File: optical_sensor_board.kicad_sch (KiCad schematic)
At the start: 34 parts, among them J2 Conn_01x09_Socket, U1 PMW3389DM‐T3QU, U3 LM317L_SOT-89

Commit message: start TestPoint routing
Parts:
- TP1, TP10, TP11, TP12, TP13, TP14, TP15, TP16, TP2, TP3, TP4, TP5, TP6, TP7, TP8, TP9: footprint TestPoint:TestPoint_Keystone_5019_Miniature -> TestPoint:TestPoint_Pad_1.0x1.0mm
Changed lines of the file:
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@@
 			)
 		)
-		(property "Footprint" "TestPoint:TestPoint_Keystone_5019_Miniature"
+		(property "Footprint" "TestPoint:TestPoint_Pad_1.0x1.0mm"
 			(at 203.2 144.78 0)
 			(effects
@@
 			)
 		)
-		(property "Footprint" "TestPoint:TestPoint_Keystone_5019_Miniature"
+		(property "Footprint" "TestPoint:TestPoint_Pad_1.0x1.0mm"
 			(at 101.6 101.6 0)
 			(effects
@@
 			)
 		)
-		(property "Footprint" "TestPoint:TestPoint_Keystone_5019_Miniature"
+		(property "Footprint" "TestPoint:TestPoint_Pad_1.0x1.0mm"
 			(at 266.7 129.54 0)
 			(effects
@@
 			)
 		)
-		(property "Footprint" "TestPoint:TestPoint_Keystone_5019_Miniature"
+		(property "Footprint" "TestPoint:TestPoint_Pad_1.0x1.0mm"
 			(at 101.6 78.74 0)
 			(effects
@@
 			)
 		)
-		(property "Footprint" "TestPoint:TestPoint_Keystone_5019_Miniature"
+		(property "Footprint" "TestPoint:TestPoint_Pad_1.0x1.0mm"
 			(at 190.5 129.54 0)
 			(effects
@@
 			)
 		)
-		(property "Footprint" "TestPoint:TestPoint_Keystone_5019_Miniature"
+		(property "Footprint" "TestPoint:TestPoint_Pad_1.0x1.0mm"
 			(at 254 129.54 0)
 			(effects
@@
 			)
 		)
-		(property "Footprint" "TestPoint:TestPoint_Keystone_5019_Miniature"
+		(property "Footprint" "TestPoint:TestPoint_Pad_1.0x1.0mm"
 			(at 194.31 41.91 0)
 			(effects
@@
 			)
 		)
-		(property "Footprint" "TestPoint:TestPoint_Keystone_5019_Miniature"
+		(property "Footprint" "TestPoint:TestPoint_Pad_1.0x1.0mm"
 			(at 215.9 129.54 0)
 			(effects
@@
 			)
 		)
-		(property "Footprint" "TestPoint:TestPoint_Keystone_5019_Miniature"
+		(property "Footprint" "TestPoint:TestPoint_Pad_1.0x1.0mm"
 			(at 69.85 153.67 0)
 			(effects
@@
 			)
 		)
-		(property "Footprint" "TestPoint:TestPoint_Keystone_5019_Miniature"
+		(property "Footprint" "TestPoint:TestPoint_Pad_1.0x1.0mm"
 			(at 190.5 144.78 0)
 			(effects
@@
 			)
 		)
-		(property "Footprint" "TestPoint:TestPoint_Keystone_5019_Miniature"
+		(property "Footprint" "TestPoint:TestPoint_Pad_1.0x1.0mm"
 			(at 241.3 129.54 0)
 			(effects
@@
 			)
 		)
-		(property "Footprint" "TestPoint:TestPoint_Keystone_5019_Miniature"
+		(property "Footprint" "TestPoint:TestPoint_Pad_1.0x1.0mm"
 			(at 124.46 57.15 0)
 			(effects
@@
 			)
 		)
-		(property "Footprint" "TestPoint:TestPoint_Keystone_5019_Miniature"
+		(property "Footprint" "TestPoint:TestPoint_Pad_1.0x1.0mm"
 			(at 228.6 129.54 0)
 			(effects
@@
 			)
 		)
-		(property "Footprint" "TestPoint:TestPoint_Keystone_5019_Miniature"
+		(property "Footprint" "TestPoint:TestPoint_Pad_1.0x1.0mm"
 			(at 143.51 57.15 0)
 			(effects
@@
 			)
 		)
-		(property "Footprint" "TestPoint:TestPoint_Keystone_5019_Miniature"
+		(property "Footprint" "TestPoint:TestPoint_Pad_1.0x1.0mm"
 			(at 203.2 129.54 0)
 			(effects
@@
 			)
 		)
-		(property "Footprint" "TestPoint:TestPoint_Keystone_5019_Miniature"
+		(property "Footprint" "TestPoint:TestPoint_Pad_1.0x1.0mm"
 			(at 97.79 132.08 0)
 			(effects

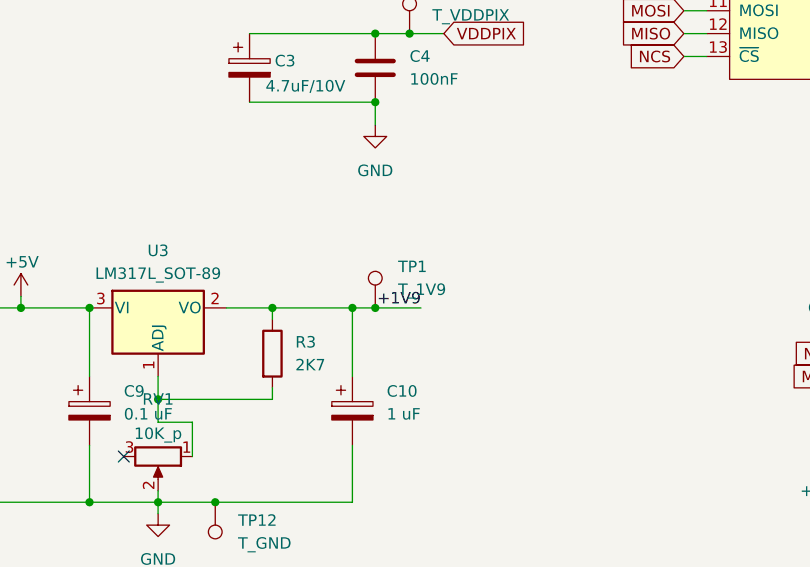
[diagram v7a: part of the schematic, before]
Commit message: TestPoint routed
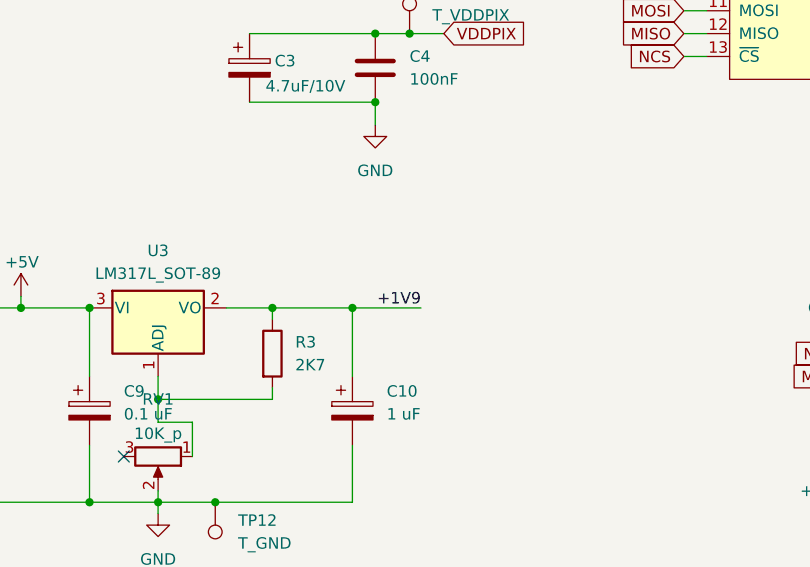
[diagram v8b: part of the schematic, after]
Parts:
- removed TP1: T_1V9, TestPoint:TestPoint_Pad_1.0x1.0mm, symbol Connector:TestPoint
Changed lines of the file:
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@@
 		(color 0 0 0 0)
 	)
-	(junction
-		(at 92.71 132.08)
-		(diameter 0)
-		(color 0 0 0 0)
-	)
 	(no_connect
 		(at 64.77 148.59)
@@
 	(wire
 		(pts
-			(xy 92.71 132.08) (xy 97.79 132.08)
+			(xy 90.17 132.08) (xy 97.79 132.08)
 		)
 		(stroke
@@
 	(wire
 		(pts
-			(xy 90.17 132.08) (xy 92.71 132.08)
-		)
-		(stroke
-			(width 0)
-			(type default)
-		)
-	)
-	(wire
-		(pts
 			(xy 151.13 144.78) (xy 148.59 144.78)
 		)
@@
 					(unit 1)
 				)
-			)
-		)
-	)
-	(symbol
-		(lib_id "Connector:TestPoint")
-		(at 92.71 132.08 0)
-		(unit 1)
-		(exclude_from_sim no)
-		(in_bom yes)
-		(on_board yes)
-		(dnp no)
-		(fields_autoplaced yes)
-		(property "Reference" "TP1"
-			(at 95.25 127.5079 0)
-			(effects
-				(font
-					(size 1.27 1.27)
-				)
-				(justify left)
-			)
-		)
-		(property "Value" "T_1V9"
-			(at 95.25 130.0479 0)
-			(effects
-				(font
-					(size 1.27 1.27)
-				)
-				(justify left)
-			)
-		)
-		(property "Footprint" "TestPoint:TestPoint_Pad_1.0x1.0mm"
-			(at 97.79 132.08 0)
-			(effects
-				(font
-					(size 1.27 1.27)
-				)
-				(hide yes)
-			)
-		)
-		(property "Datasheet" "~"
-			(at 97.79 132.08 0)
-			(effects
-				(font
-					(size 1.27 1.27)
-				)
-				(hide yes)
-			)
-		)
-		(property "Description" "test point"
-			(at 92.71 132.08 0)
-			(effects
-				(font
-					(size 1.27 1.27)
-				)
-				(hide yes)
-			)
-		)
-		(pin "1"
-		)
-		(instances
-			(project ""
-				(path "/bc898632-37cb-47d1-8655-c4a22efc7ca2"
-					(reference "TP1")
-					(unit 1)
-				)
